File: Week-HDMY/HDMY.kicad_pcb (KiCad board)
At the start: 2 copper layers, 26 parts, among them J1 HDMI_A, J2 HDMI_A, J3 HDMI_A, J4 Conn_01x10, U1 TS3DV421, U2 AP7333-33SRG-7, U3 AP7333-15SRG-7

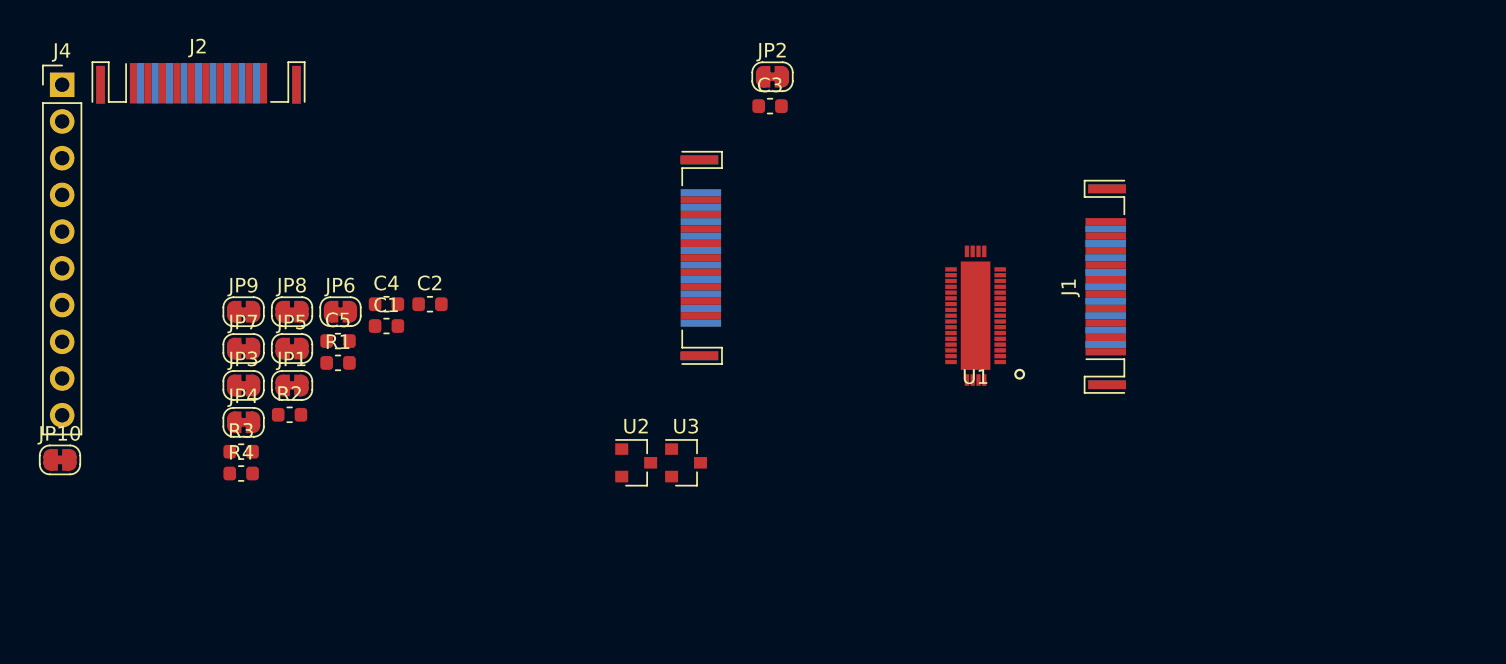
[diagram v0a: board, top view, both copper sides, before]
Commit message: differential traces done on hdmy
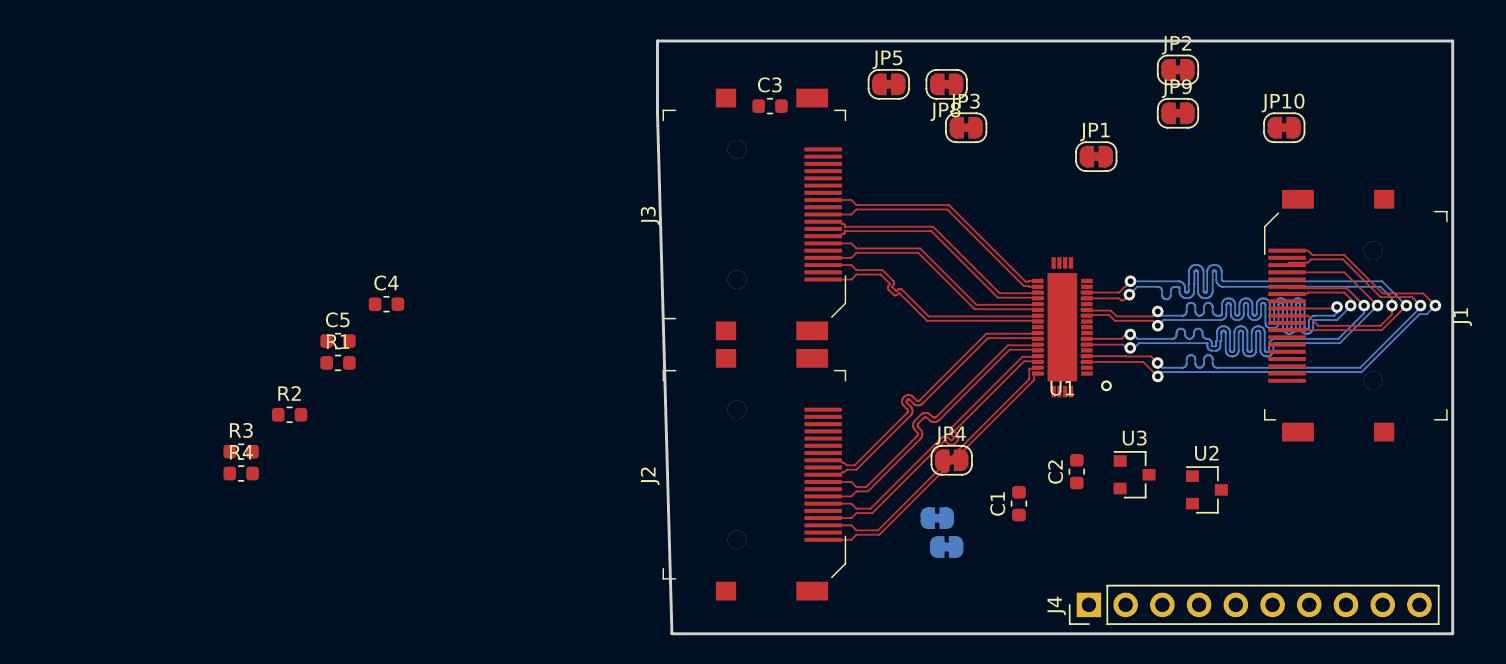
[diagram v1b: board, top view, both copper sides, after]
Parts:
- J1, J2: footprint Connector_HDMI:HDMI_A_Contact_Technology_HDMI-19APL2_Horizontal -> digikey-footprints:HDMI_A_Female_2000-1-2-41-00-BK
- J3: footprint Connector_HDMI:HDMI_A_Contact_Technology_HDMI-19APL2_Horizontal -> digikey-footprints:HDMI_A_Female_2000-1-2-41-00-BK; moved to F.Cu
- JP6, JP7: moved to B.Cu
- moved JP10 87.7 mm to (206.3, 102.0)
- moved J4 79.6 mm to (192.8, 135.0), turned to 90 degrees
- moved JP9 66.1 mm to (199.0, 101.0)
- moved JP1 57.8 mm to (193.3, 104.0)
- moved JP3 53.1 mm to (184.3, 102.0)
- moved JP7 50.5 mm to (183.0, 131.0), turned to 180 degrees
- moved JP4 49.0 mm to (183.3, 125.0)
- moved JP8 47.9 mm to (183.0, 99.0), turned to 180 degrees
- moved J2 47.3 mm to (170.0, 126.0), turned to 90 degrees
- moved C2 46.2 mm to (192.0, 125.8), turned to 90 degrees
- moved C1 45.4 mm to (188.0, 128.0), turned to 90 degrees
- moved JP5 45.1 mm to (179.0, 99.0)
- moved JP6 43.7 mm to (182.3, 129.0), turned to 180 degrees
- moved U2 39.5 mm to (201.0, 127.0)
- moved U3 31.0 mm to (196.0, 126.0)
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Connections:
- U1 pad 43: GND -> (no net)
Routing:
- net /OUTD1-: track 0.00 -> 38.9 mm, vias 0 -> 2
- net /OUTD1+: track 0.00 -> 38.9 mm, vias 0 -> 2
- net /OUTCLK-: track 0.00 -> 38.9 mm, vias 0 -> 2
- net /OUTCLK+: track 0.00 -> 38.9 mm, vias 0 -> 2
- net /OUTD0-: track 0.00 -> 38.9 mm, vias 0 -> 2
- net /OUTD0+: track 0.00 -> 38.9 mm, vias 0 -> 2
- net /OUTD2-: track 0.00 -> 38.8 mm, vias 0 -> 2
- net /OUTD2+: track 0.00 -> 38.8 mm, vias 0 -> 2
- net /INAD1-: track 0.00 -> 20.6 mm
- net /INAD1+: track 0.00 -> 20.6 mm
- net /INAD0+: track 0.00 -> 20.6 mm
- net /INAD0-: track 0.00 -> 20.6 mm
- net /INAD2+: track 0.00 -> 20.5 mm
- net /INACLK+: track 0.00 -> 20.5 mm
- net /INACLK-: track 0.00 -> 20.5 mm
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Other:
- board outline added: 55 x 41 mm
- net class Default: clearance 0.2 -> 0.127; trace_width 0.25 -> 0.127
- rule trace_clearance: 0.2 -> 0.127
- rule trace_min: 0.2 -> 0.127

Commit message: end of week push
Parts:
- JP1, JP4, JP5: moved to B.Cu
- moved R4 65.4 mm to (199.5, 130.8)
- moved C4 45.3 mm to (188.5, 124.0)
- moved JP5 31.9 mm to (187.5, 129.8)
- moved JP3 25.2 mm to (192.1, 126.0)
- moved JP1 24.9 mm to (183.8, 127.0), turned to 180 degrees
- moved JP8 11.0 mm to (191.1, 106.5)
- moved R3 9.28 mm to (143.5, 125.0)
- moved JP4 7.51 mm to (183.8, 132.5), turned to 180 degrees
- moved JP9 5.65 mm to (196.9, 106.2)
- moved C1 4.56 mm to (192.5, 127.3)
- moved JP7 4.32 mm to (183.8, 135.2)
- moved R2 3.77 mm to (141.0, 120.2)
- moved U2 3.53 mm to (199.8, 123.8)
- moved JP6 1.59 mm to (183.8, 129.8)
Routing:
- net GND: track 0.00 -> 37.3 mm, vias 0 -> 11
- net /OUTUTIL: track 0.00 -> 26.2 mm, vias 0 -> 1
- net /OUTSCL: track 0.00 -> 25.2 mm
- net /INASDA: track 0.00 -> 23.6 mm, vias 0 -> 1
- net /INAUTIL: track 0.00 -> 23.6 mm, vias 0 -> 1
- net /INASCL: track 0.00 -> 21.9 mm, vias 0 -> 1
- net /OUTCEC: track 0.00 -> 21.2 mm
- net /OUTSDA: track 0.00 -> 20.4 mm
- net /OUTHBD: track 0.00 -> 18.9 mm
